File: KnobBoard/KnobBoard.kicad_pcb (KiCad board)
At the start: 2 copper layers, 45.7 x 15.2 mm, 4 parts, among them J1 Conn_01x04_MountingPin, J2 Conn_01x02_Female, SW1 Rotary_Encoder_Switch, SW2 Rotary_Encoder_Switch

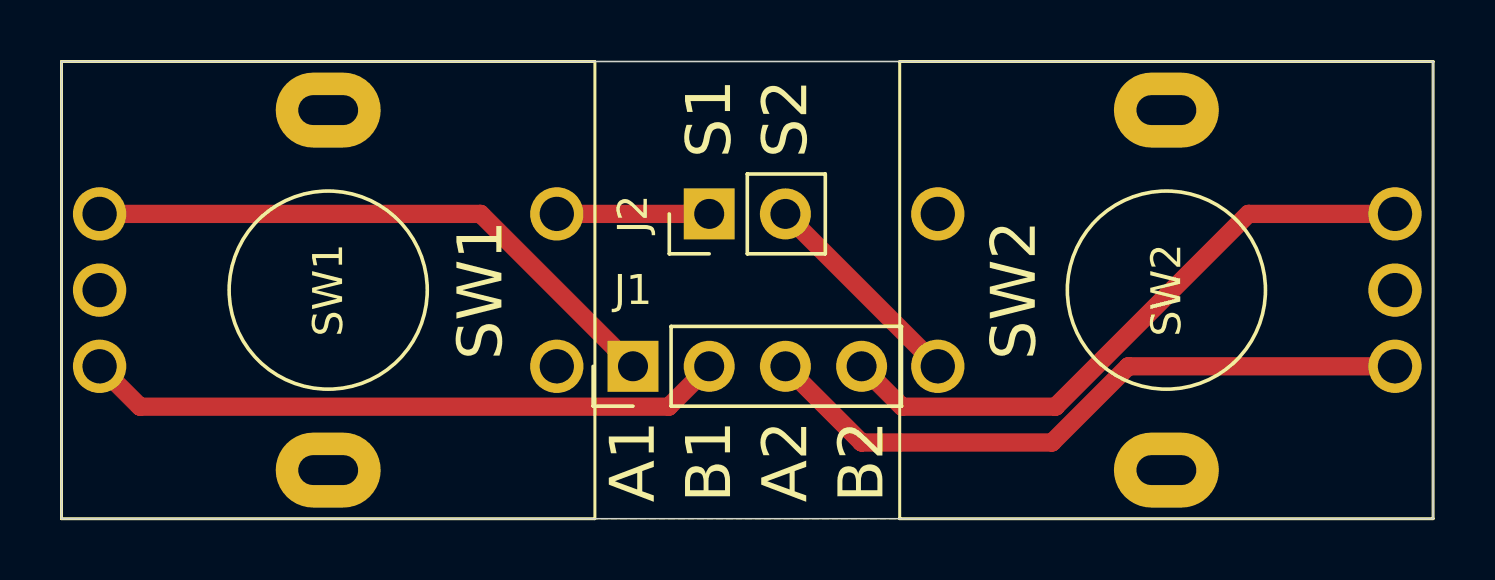
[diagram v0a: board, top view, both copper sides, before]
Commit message: Adding Docs and updates to footprints
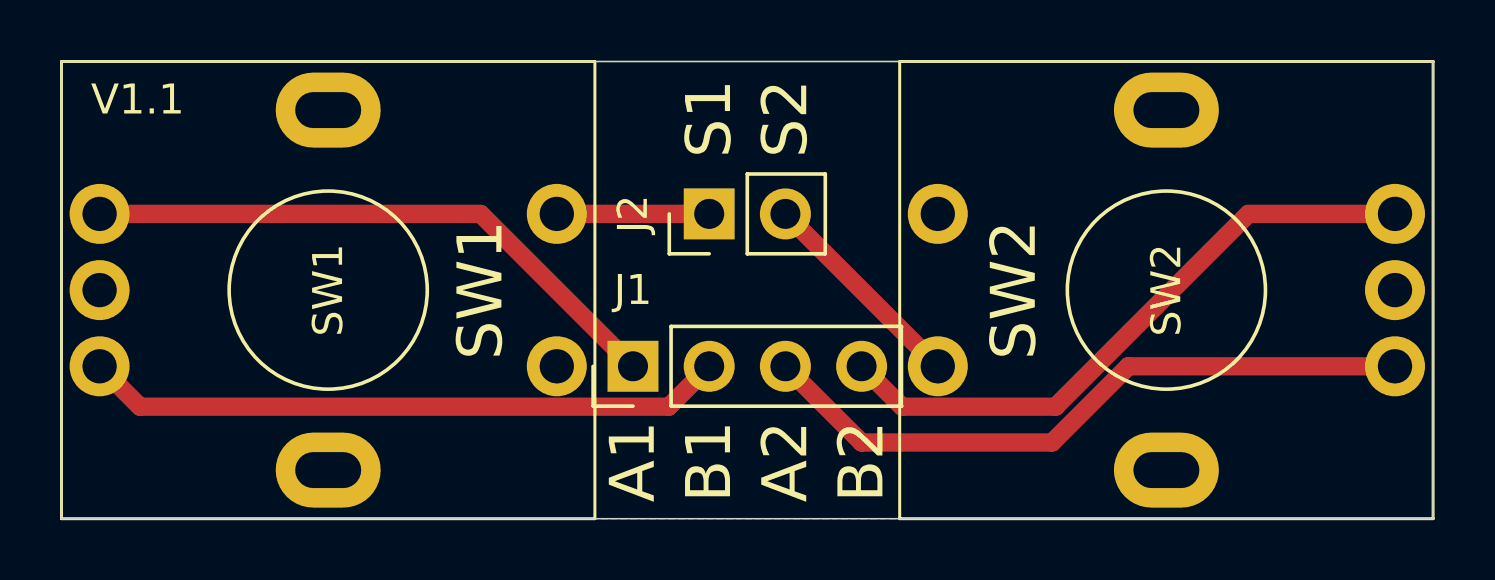
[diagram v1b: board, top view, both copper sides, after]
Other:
- board text added: "V1.1"
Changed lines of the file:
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@@
   (general
     (thickness 1.6)
-    (drawings 27)
+    (drawings 29)
     (tracks 15)
     (zones 0)
@@
   (title_block
     (title "Rotary Encoder Board, 12mm with SPST")
-    (date 2021-10-11)
-    (rev 1.0)
+    (date 2021-10-25)
+    (rev 1.1)
   )
   (layers
@@
   )
   (module KnobBoard:KSA_Tactile_SPST_12mm (layer F.Cu)
+    (at 63.5 50.8 270)
+    (descr "KSA http://www.ckswitches.com/media/1457/ksa_ksl.pdf")
+    (tags "SWITCH SMD KSA SW")
+    (fp_text reference SW1 (at 0 0 90) (layer F.SilkS)
+      (effects (font (size 1 1) (thickness 0.15)))
+    )
+    (fp_text value Rotary_Encoder_Switch (at 0 1.524 90) (layer F.Fab)
+      (effects (font (size 1 1) (thickness 0.15)))
+    )
+    (fp_circle (center 0 0) (end 3.302 0) (layer B.SilkS) (width 0.1))
+    (fp_line (start 5.75 -5.75) (end -5.75 -5.75) (layer F.CrtYd) (width 0.12))
+    (fp_line (start 5.75 5.75) (end 5.75 -5.75) (layer F.CrtYd) (width 0.12))
+    (fp_line (start -5.75 5.75) (end 5.75 5.75) (layer F.CrtYd) (width 0.12))
+    (fp_line (start -5.75 -5.75) (end -5.75 5.75) (layer F.CrtYd) (width 0.12))
+    (fp_line (start -7.62 8.89) (end -7.62 -8.89) (layer F.SilkS) (width 0.1))
+    (fp_line (start 7.62 8.89) (end -7.62 8.89) (layer F.SilkS) (width 0.1))
+    (fp_line (start 7.62 -8.89) (end 7.62 8.89) (layer F.SilkS) (width 0.1))
+    (fp_line (start -7.62 -8.89) (end 7.62 -8.89) (layer F.SilkS) (width 0.1))
+    (fp_line (start 3.7 4.1) (end 3.7 -4.1) (layer F.Fab) (width 0.1))
+    (fp_circle (center 0 0) (end 3.302 0) (layer F.SilkS) (width 0.12))
+    (fp_line (start -3.7 4.1) (end -3.7 -4.1) (layer F.Fab) (width 0.1))
+    (fp_line (start 3.7 -4.1) (end -3.7 -4.1) (layer F.Fab) (width 0.1))
+    (fp_line (start -3.7 4.1) (end 3.7 4.1) (layer F.Fab) (width 0.1))
+    (fp_text user %R (at 0 0 90) (layer F.Fab)
+      (effects (font (size 1 1) (thickness 0.15)))
+    )
+    (pad G thru_hole oval (at -6 0 270) (size 2.5 3.5) (drill oval 1.2 2.2) (layers *.Cu *.Mask))
+    (pad G thru_hole oval (at 6 0 270) (size 2.5 3.5) (drill oval 1.2 2.2) (layers *.Cu *.Mask))
+    (pad S1 thru_hole circle (at -2.54 -7.62 270) (size 2 2) (drill 1.143) (layers *.Cu *.Mask)
+      (net 6 /SW1))
+    (pad S2 thru_hole circle (at 2.54 -7.62 270) (size 2 2) (drill 1.143) (layers *.Cu *.Mask)
+      (net 7 GND))
+    (pad B thru_hole circle (at 2.54 7.62 270) (size 2 2) (drill 1.143) (layers *.Cu *.Mask)
+      (net 3 /B1))
+    (pad C thru_hole circle (at 0 7.62 270) (size 2 2) (drill 1.143) (layers *.Cu *.Mask)
+      (net 7 GND))
+    (pad A thru_hole circle (at -2.54 7.62 270) (size 2 2) (drill 1.143) (layers *.Cu *.Mask)
+      (net 4 /A1))
+    (model ${KISYS3DMOD}/Buttons_Switches_THT.3dshapes/KSA_Tactile_SPST.wrl
+      (at (xyz 0 0 0))
+      (scale (xyz 1 1 1))
+      (rotate (xyz 0 0 0))
+    )
+  )
+  (module KnobBoard:KSA_Tactile_SPST_12mm (layer F.Cu)
     (at 91.44 50.8 90)
     (descr "KSA http://www.ckswitches.com/media/1457/ksa_ksl.pdf")
@@
       (effects (font (size 1 1) (thickness 0.15)))
     )
+    (fp_circle (center 0 0) (end 3.302 0) (layer B.SilkS) (width 0.1))
+    (fp_line (start 5.75 -5.75) (end -5.75 -5.75) (layer F.CrtYd) (width 0.12))
+    (fp_line (start 5.75 5.75) (end 5.75 -5.75) (layer F.CrtYd) (width 0.12))
+    (fp_line (start -5.75 5.75) (end 5.75 5.75) (layer F.CrtYd) (width 0.12))
+    (fp_line (start -5.75 -5.75) (end -5.75 5.75) (layer F.CrtYd) (width 0.12))
+    (fp_line (start -7.62 8.89) (end -7.62 -8.89) (layer F.SilkS) (width 0.1))
+    (fp_line (start 7.62 8.89) (end -7.62 8.89) (layer F.SilkS) (width 0.1))
+    (fp_line (start 7.62 -8.89) (end 7.62 8.89) (layer F.SilkS) (width 0.1))
+    (fp_line (start -7.62 -8.89) (end 7.62 -8.89) (layer F.SilkS) (width 0.1))
+    (fp_line (start 3.7 4.1) (end 3.7 -4.1) (layer F.Fab) (width 0.1))
+    (fp_circle (center 0 0) (end 3.302 0) (layer F.SilkS) (width 0.12))
+    (fp_line (start -3.7 4.1) (end -3.7 -4.1) (layer F.Fab) (width 0.1))
+    (fp_line (start 3.7 -4.1) (end -3.7 -4.1) (layer F.Fab) (width 0.1))
+    (fp_line (start -3.7 4.1) (end 3.7 4.1) (layer F.Fab) (width 0.1))
     (fp_text user %R (at 0 0 90) (layer F.Fab)
       (effects (font (size 1 1) (thickness 0.15)))
     )
-    (fp_line (start -3.7 4.1) (end 3.7 4.1) (layer F.Fab) (width 0.1))
-    (fp_line (start 3.7 -4.1) (end -3.7 -4.1) (layer F.Fab) (width 0.1))
-    (fp_line (start -3.7 4.1) (end -3.7 -4.1) (layer F.Fab) (width 0.1))
-    (fp_circle (center 0 0) (end 3.302 0) (layer F.SilkS) (width 0.12))
-    (fp_line (start 3.7 4.1) (end 3.7 -4.1) (layer F.Fab) (width 0.1))
-    (fp_line (start -7.62 -8.89) (end 7.62 -8.89) (layer F.SilkS) (width 0.1))
-    (fp_line (start 7.62 -8.89) (end 7.62 8.89) (layer F.SilkS) (width 0.1))
-    (fp_line (start 7.62 8.89) (end -7.62 8.89) (layer F.SilkS) (width 0.1))
-    (fp_line (start -7.62 8.89) (end -7.62 -8.89) (layer F.SilkS) (width 0.1))
-    (fp_line (start -5.75 -5.75) (end -5.75 5.75) (layer F.CrtYd) (width 0.12))
-    (fp_line (start -5.75 5.75) (end 5.75 5.75) (layer F.CrtYd) (width 0.12))
-    (fp_line (start 5.75 5.75) (end 5.75 -5.75) (layer F.CrtYd) (width 0.12))
-    (fp_line (start 5.75 -5.75) (end -5.75 -5.75) (layer F.CrtYd) (width 0.12))
-    (fp_circle (center 0 0) (end 3.302 0) (layer B.SilkS) (width 0.1))
-    (pad G thru_hole oval (at -6 0 90) (size 2.5 3.5) (drill oval 1 2) (layers *.Cu *.Mask))
-    (pad G thru_hole oval (at 6 0 90) (size 2.5 3.5) (drill oval 1 2) (layers *.Cu *.Mask))
-    (pad S1 thru_hole circle (at -2.54 -7.62 90) (size 1.778 1.778) (drill 1.143) (layers *.Cu *.Mask)
+    (pad G thru_hole oval (at -6 0 90) (size 2.5 3.5) (drill oval 1.2 2.2) (layers *.Cu *.Mask))
+    (pad G thru_hole oval (at 6 0 90) (size 2.5 3.5) (drill oval 1.2 2.2) (layers *.Cu *.Mask))
+    (pad S1 thru_hole circle (at -2.54 -7.62 90) (size 2 2) (drill 1.143) (layers *.Cu *.Mask)
       (net 5 /SW2))
-    (pad S2 thru_hole circle (at 2.54 -7.62 90) (size 1.778 1.778) (drill 1.143) (layers *.Cu *.Mask)
-      (net 7 GND))
-    (pad B thru_hole circle (at 2.54 7.62 90) (size 1.778 1.778) (drill 1.143) (layers *.Cu *.Mask)
+    (pad S2 thru_hole circle (at 2.54 -7.62 90) (size 2 2) (drill 1.143) (layers *.Cu *.Mask)
+      (net 7 GND))
+    (pad B thru_hole circle (at 2.54 7.62 90) (size 2 2) (drill 1.143) (layers *.Cu *.Mask)
       (net 1 /B2))
-    (pad C thru_hole circle (at 0 7.62 90) (size 1.778 1.778) (drill 1.143) (layers *.Cu *.Mask)
-      (net 7 GND))
-    (pad A thru_hole circle (at -2.54 7.62 90) (size 1.778 1.778) (drill 1.143) (layers *.Cu *.Mask)
+    (pad C thru_hole circle (at 0 7.62 90) (size 2 2) (drill 1.143) (layers *.Cu *.Mask)
+      (net 7 GND))
+    (pad A thru_hole circle (at -2.54 7.62 90) (size 2 2) (drill 1.143) (layers *.Cu *.Mask)
       (net 2 /A2))
-    (model ${KISYS3DMOD}/Buttons_Switches_THT.3dshapes/KSA_Tactile_SPST.wrl
-      (at (xyz 0 0 0))
-      (scale (xyz 1 1 1))
-      (rotate (xyz 0 0 0))
-    )
-  )
-  (module KnobBoard:KSA_Tactile_SPST_12mm (layer F.Cu)
-    (at 63.5 50.8 270)
-    (descr "KSA http://www.ckswitches.com/media/1457/ksa_ksl.pdf")
-    (tags "SWITCH SMD KSA SW")
-    (fp_text reference SW1 (at 0 0 90) (layer F.SilkS)
-      (effects (font (size 1 1) (thickness 0.15)))
-    )
-    (fp_text value Rotary_Encoder_Switch (at 0 1.524 90) (layer F.Fab)
-      (effects (font (size 1 1) (thickness 0.15)))
-    )
-    (fp_text user %R (at 0 0 90) (layer F.Fab)
-      (effects (font (size 1 1) (thickness 0.15)))
-    )
-    (fp_line (start -3.7 4.1) (end 3.7 4.1) (layer F.Fab) (width 0.1))
-    (fp_line (start 3.7 -4.1) (end -3.7 -4.1) (layer F.Fab) (width 0.1))
-    (fp_line (start -3.7 4.1) (end -3.7 -4.1) (layer F.Fab) (width 0.1))
-    (fp_circle (center 0 0) (end 3.302 0) (layer F.SilkS) (width 0.12))
-    (fp_line (start 3.7 4.1) (end 3.7 -4.1) (layer F.Fab) (width 0.1))
-    (fp_line (start -7.62 -8.89) (end 7.62 -8.89) (layer F.SilkS) (width 0.1))
-    (fp_line (start 7.62 -8.89) (end 7.62 8.89) (layer F.SilkS) (width 0.1))
-    (fp_line (start 7.62 8.89) (end -7.62 8.89) (layer F.SilkS) (width 0.1))
-    (fp_line (start -7.62 8.89) (end -7.62 -8.89) (layer F.SilkS) (width 0.1))
-    (fp_line (start -5.75 -5.75) (end -5.75 5.75) (layer F.CrtYd) (width 0.12))
-    (fp_line (start -5.75 5.75) (end 5.75 5.75) (layer F.CrtYd) (width 0.12))
-    (fp_line (start 5.75 5.75) (end 5.75 -5.75) (layer F.CrtYd) (width 0.12))
-    (fp_line (start 5.75 -5.75) (end -5.75 -5.75) (layer F.CrtYd) (width 0.12))
-    (fp_circle (center 0 0) (end 3.302 0) (layer B.SilkS) (width 0.1))
-    (pad G thru_hole oval (at -6 0 270) (size 2.5 3.5) (drill oval 1 2) (layers *.Cu *.Mask))
-    (pad G thru_hole oval (at 6 0 270) (size 2.5 3.5) (drill oval 1 2) (layers *.Cu *.Mask))
-    (pad S1 thru_hole circle (at -2.54 -7.62 270) (size 1.778 1.778) (drill 1.143) (layers *.Cu *.Mask)
-      (net 6 /SW1))
-    (pad S2 thru_hole circle (at 2.54 -7.62 270) (size 1.778 1.778) (drill 1.143) (layers *.Cu *.Mask)
-      (net 7 GND))
-    (pad B thru_hole circle (at 2.54 7.62 270) (size 1.778 1.778) (drill 1.143) (layers *.Cu *.Mask)
-      (net 3 /B1))
-    (pad C thru_hole circle (at 0 7.62 270) (size 1.778 1.778) (drill 1.143) (layers *.Cu *.Mask)
-      (net 7 GND))
-    (pad A thru_hole circle (at -2.54 7.62 270) (size 1.778 1.778) (drill 1.143) (layers *.Cu *.Mask)
-      (net 4 /A1))
     (model ${KISYS3DMOD}/Buttons_Switches_THT.3dshapes/KSA_Tactile_SPST.wrl
       (at (xyz 0 0 0))
@@
     )
   )
+  (gr_text V1.1 (at 57.15 44.45) (layer F.SilkS)
+    (effects (font (size 1 1) (thickness 0.15)))
+  )
+  (gr_text V1.1 (at 97.79 44.45) (layer B.SilkS)
+    (effects (font (size 1 1) (thickness 0.15)) (justify mirror))
+  )
   (gr_text "Drill hole diameter > 1/4 in" (at 64.77 31.75) (layer Dwgs.User)
